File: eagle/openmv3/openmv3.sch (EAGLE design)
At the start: 64 parts, among them J3 CON_HEADER_1X03, J4 CON_HEADER_1X03, Q1 MOSFET, U12 STM32F407LQFP100, U2 USD-47571, U4 TPS768, U8 VREG_25, U9 OV2640, X2 USB-MICROB

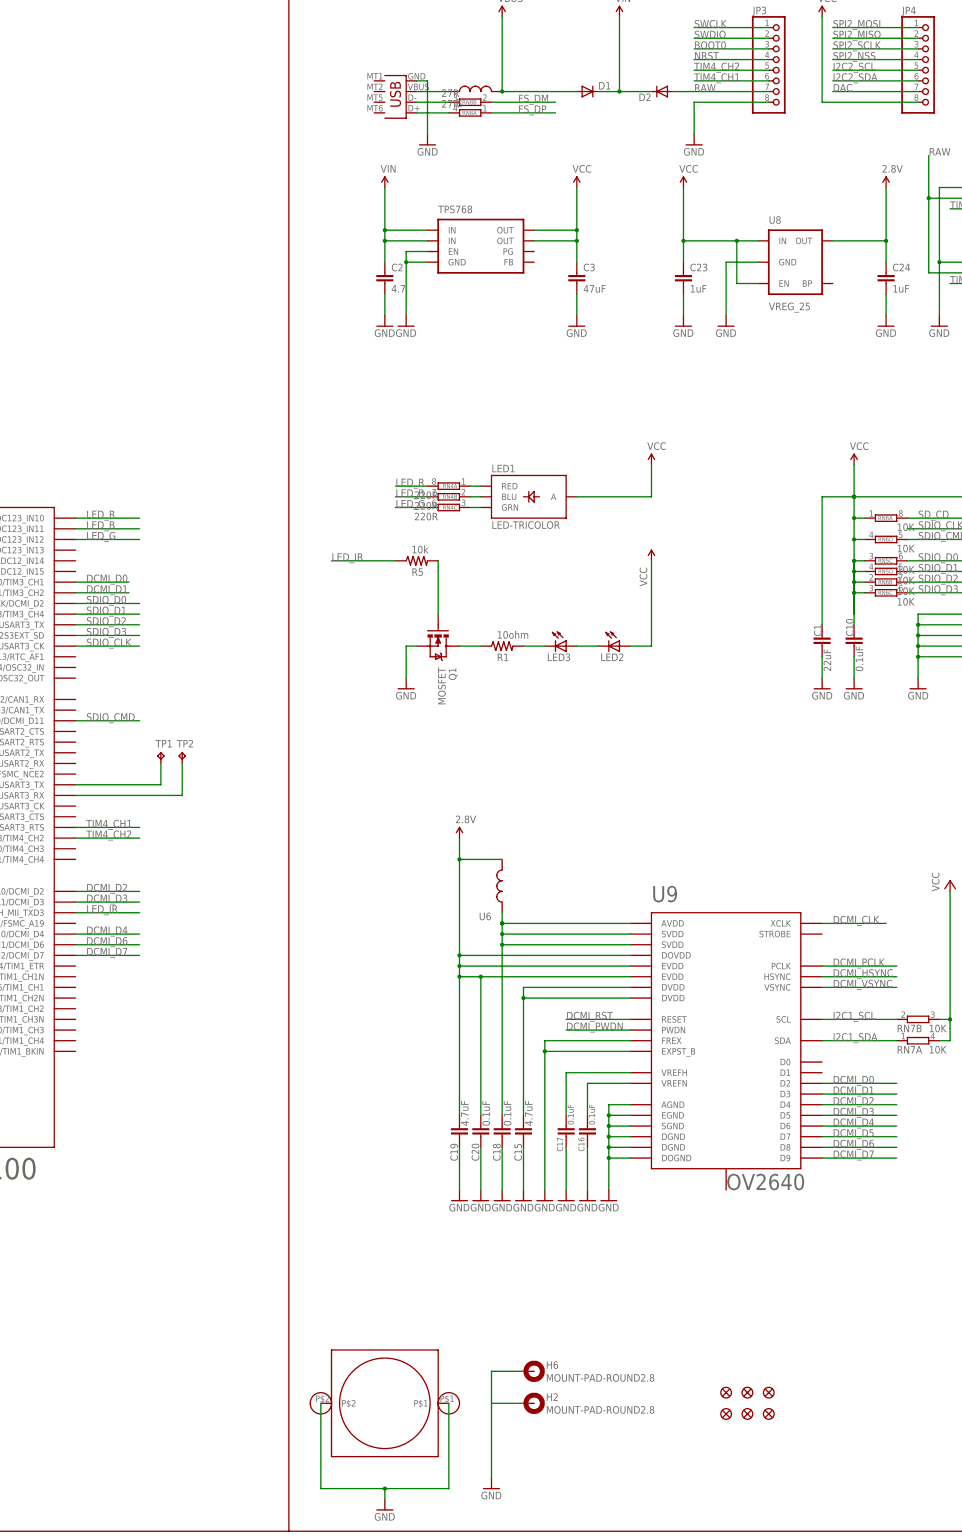
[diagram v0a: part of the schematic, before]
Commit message: Update HW
* Connect STROBE, FREX and EXPST_B
* Remove shield.
* Add pull-down to IR MOSFET
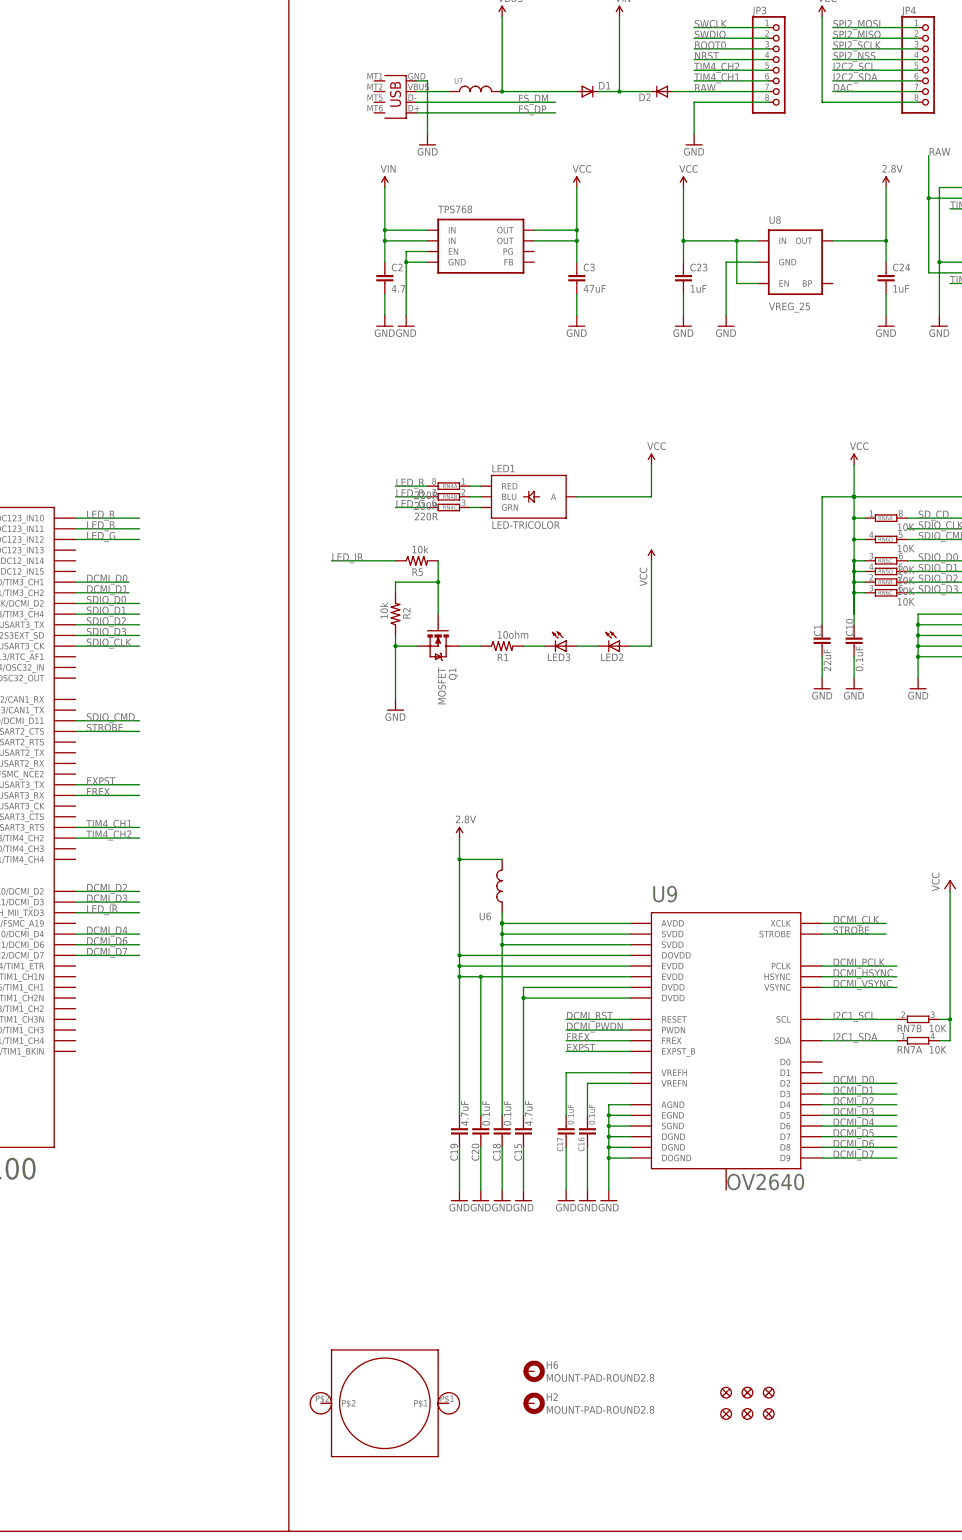
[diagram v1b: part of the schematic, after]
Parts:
- removed RN8: 27R, resistor-dil:2R-NEXBV4V
- removed TP1, TP2: TPTP12R, testpad:TPTP12R
- added R2: 10k, sfe:RESISTOR0603-RES
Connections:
- removed net N$15: RN8B.2, X2.D-
- removed net N$17: RN8A.2, X2.D+
- removed net N$19: TP1.TP, U12.PD8/FSMC_D13/USART3_TX
- removed net N$20: TP2.TP, U12.PD9/FSMC_D14/USART3_RX
- new net EXPST: U12.PD8/FSMC_D13/USART3_TX, U9.EXPST_B
- new net FREX: U12.PD9/FSMC_D14/USART3_RX, U9.FREX
- new net STROBE: U12.PD3/FSMC_CLK/USART2_CTS, U9.STROBE
- net FS_DM: now also X2.D-; no longer RN8B.1
- net FS_DP: now also X2.D+; no longer RN8A.1
- net GND: now also R2.1; no longer H2.MOUNT, H6.MOUNT, U$1.P$1, U$1.P$2, U9.EXPST_B, U9.FREX
- net N$5: now also R2.2

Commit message: Update design files
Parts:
- C2: value 4.7 -> 4.7uF
- C23, C24: value 1uF -> 4.7uF
- U8: value VREG_25 -> VREG_28
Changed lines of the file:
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@@
 <part name="GND21" library="SparkFun" deviceset="GND" device=""/>
 <part name="U$10" library="sfe" deviceset="2.8V" device=""/>
-<part name="C23" library="sfe" deviceset="CAP" device="0603-CAP" value="1uF"/>
+<part name="C23" library="sfe" deviceset="CAP" device="0603-CAP" value="4.7uF"/>
 <part name="GND27" library="SparkFun" deviceset="GND" device=""/>
-<part name="C24" library="sfe" deviceset="CAP" device="0603-CAP" value="1uF"/>
+<part name="C24" library="sfe" deviceset="CAP" device="0603-CAP" value="4.7uF"/>
 <part name="GND28" library="SparkFun" deviceset="GND" device=""/>
 <part name="U$12" library="sfe" deviceset="2.8V" device=""/>
-<part name="U8" library="sfe" deviceset="V_REG_LDO" device="SMD" value="VREG_25"/>
+<part name="U8" library="sfe" deviceset="V_REG_LDO" device="SMD" value="VREG_28"/>
 <part name="GND29" library="SparkFun" deviceset="GND" device=""/>
 <part name="P+9" library="iofault" deviceset="VIN" device=""/>
@@
 <part name="R1" library="sfe" deviceset="RESISTOR" device="0603-RES" value="10ohm"/>
 <part name="P+6" library="mux" deviceset="VCC" device=""/>
-<part name="C2" library="sfe" deviceset="CAP" device="0603-CAP" value="4.7"/>
+<part name="C2" library="sfe" deviceset="CAP" device="0603-CAP" value="4.7uF"/>
 <part name="C3" library="sfe" deviceset="CAP" device="1206" value="47uF"/>
 <part name="C11" library="sfe" deviceset="CAP" device="0805" value="22uF"/>
@@
 <instance part="C18" gate="G$1" x="304.8" y="45.72" smashed="yes">
 <attribute name="NAME" x="302.641" y="44.196" size="1.778" layer="95" rot="R270"/>
-<attribute name="VALUE" x="305.181" y="54.356" size="1.778" layer="96" rot="R270"/>
+<attribute name="VALUE" x="305.181" y="54.356" size="1.4224" layer="96" rot="R270"/>
 </instance>
 <instance part="GND17" gate="1" x="304.8" y="30.48"/>
@@
 <instance part="C19" gate="G$1" x="294.64" y="45.72" smashed="yes">
 <attribute name="NAME" x="292.481" y="44.196" size="1.778" layer="95" rot="R270"/>
-<attribute name="VALUE" x="295.021" y="54.356" size="1.778" layer="96" rot="R270"/>
+<attribute name="VALUE" x="295.021" y="54.356" size="1.4224" layer="96" rot="R270"/>
 </instance>
 <instance part="C20" gate="G$1" x="299.72" y="45.72" smashed="yes">
 <attribute name="NAME" x="297.561" y="44.196" size="1.778" layer="95" rot="R270"/>
-<attribute name="VALUE" x="300.101" y="54.356" size="1.778" layer="96" rot="R270"/>
+<attribute name="VALUE" x="300.101" y="54.356" size="1.4224" layer="96" rot="R270"/>
 </instance>
 <instance part="GND21" gate="1" x="299.72" y="30.48"/>
@@
 <instance part="C15" gate="G$1" x="309.88" y="45.72" smashed="yes">
 <attribute name="NAME" x="307.721" y="44.196" size="1.778" layer="95" rot="R270"/>
-<attribute name="VALUE" x="310.261" y="54.356" size="1.778" layer="96" rot="R270"/>
+<attribute name="VALUE" x="310.261" y="54.356" size="1.4224" layer="96" rot="R270"/>
 </instance>
 <instance part="GND12" gate="1" x="309.88" y="30.48"/>

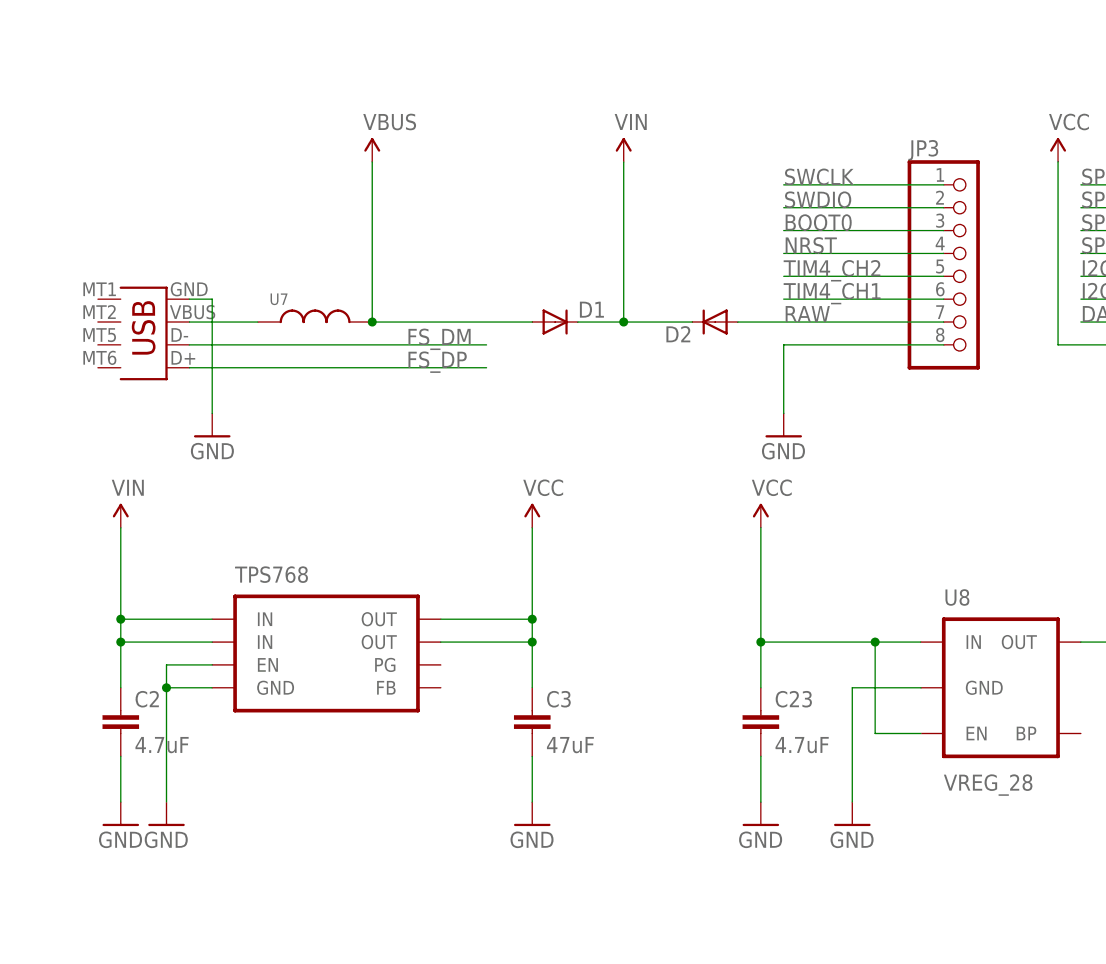
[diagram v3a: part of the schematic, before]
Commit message: Update design files
* Replace 1A TI regulator with BD 500mA.
* Replace ORing diodes with one dual common cathode.
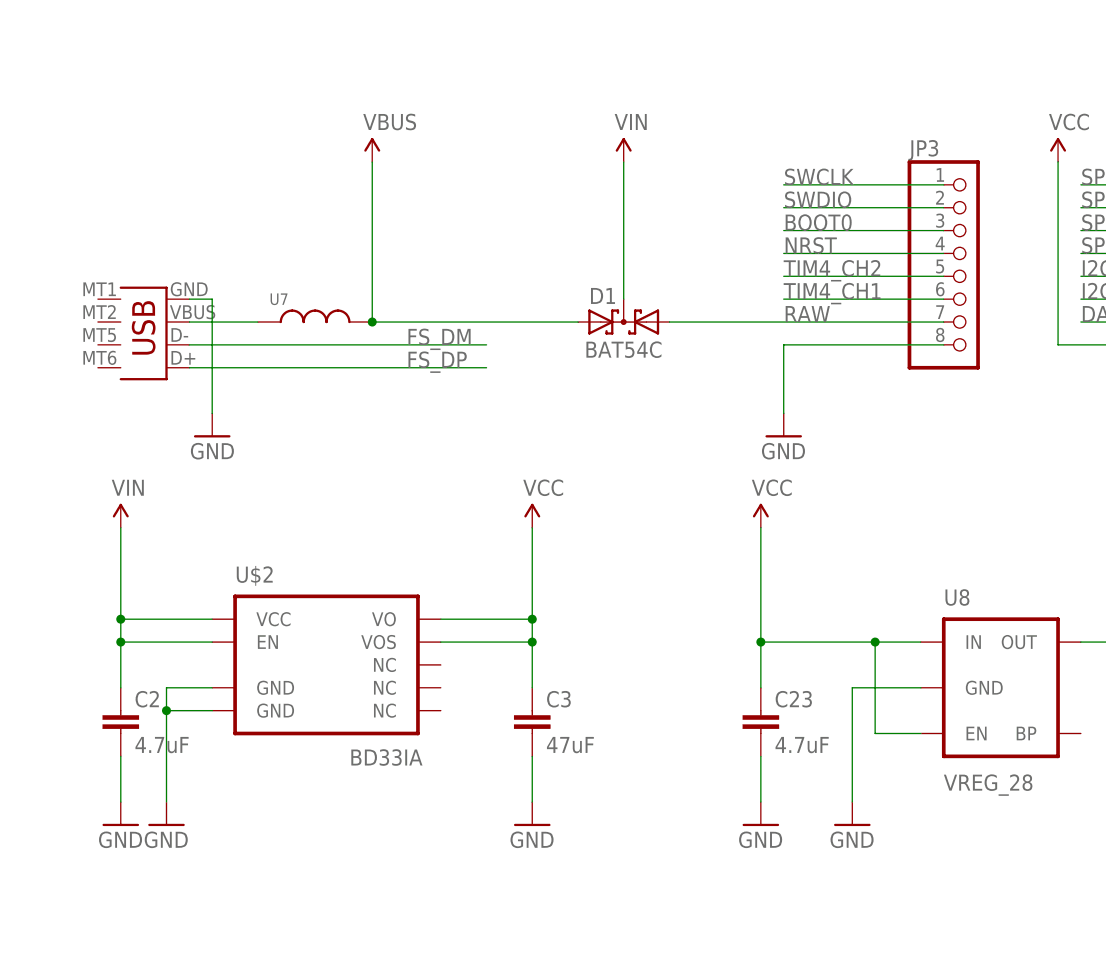
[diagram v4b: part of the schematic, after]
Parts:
- removed D2: (no value), sfe:DIODESOD
- removed U4: TPS768, mux:TPS768
- added U$2: BD33IA, mux:BD33IA
- D1: value (none) -> BAT54C; device sfe:DIODESOD -> diode:BAT54C
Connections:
- net GND: now also U$2.GND@1, U$2.GND@2; no longer U4.EN, U4.GND
- net RAW: now also D1.A1; no longer D2.A
- net VBUS: now also D1.A2; no longer D1.A
- net VCC: now also U$2.VO, U$2.VOS; no longer U4.OUT@1, U4.OUT@2
- net VIN: now also D1.CC, U$2.EN, U$2.VCC; no longer D1.C, D2.C, U4.IN@1, U4.IN@2

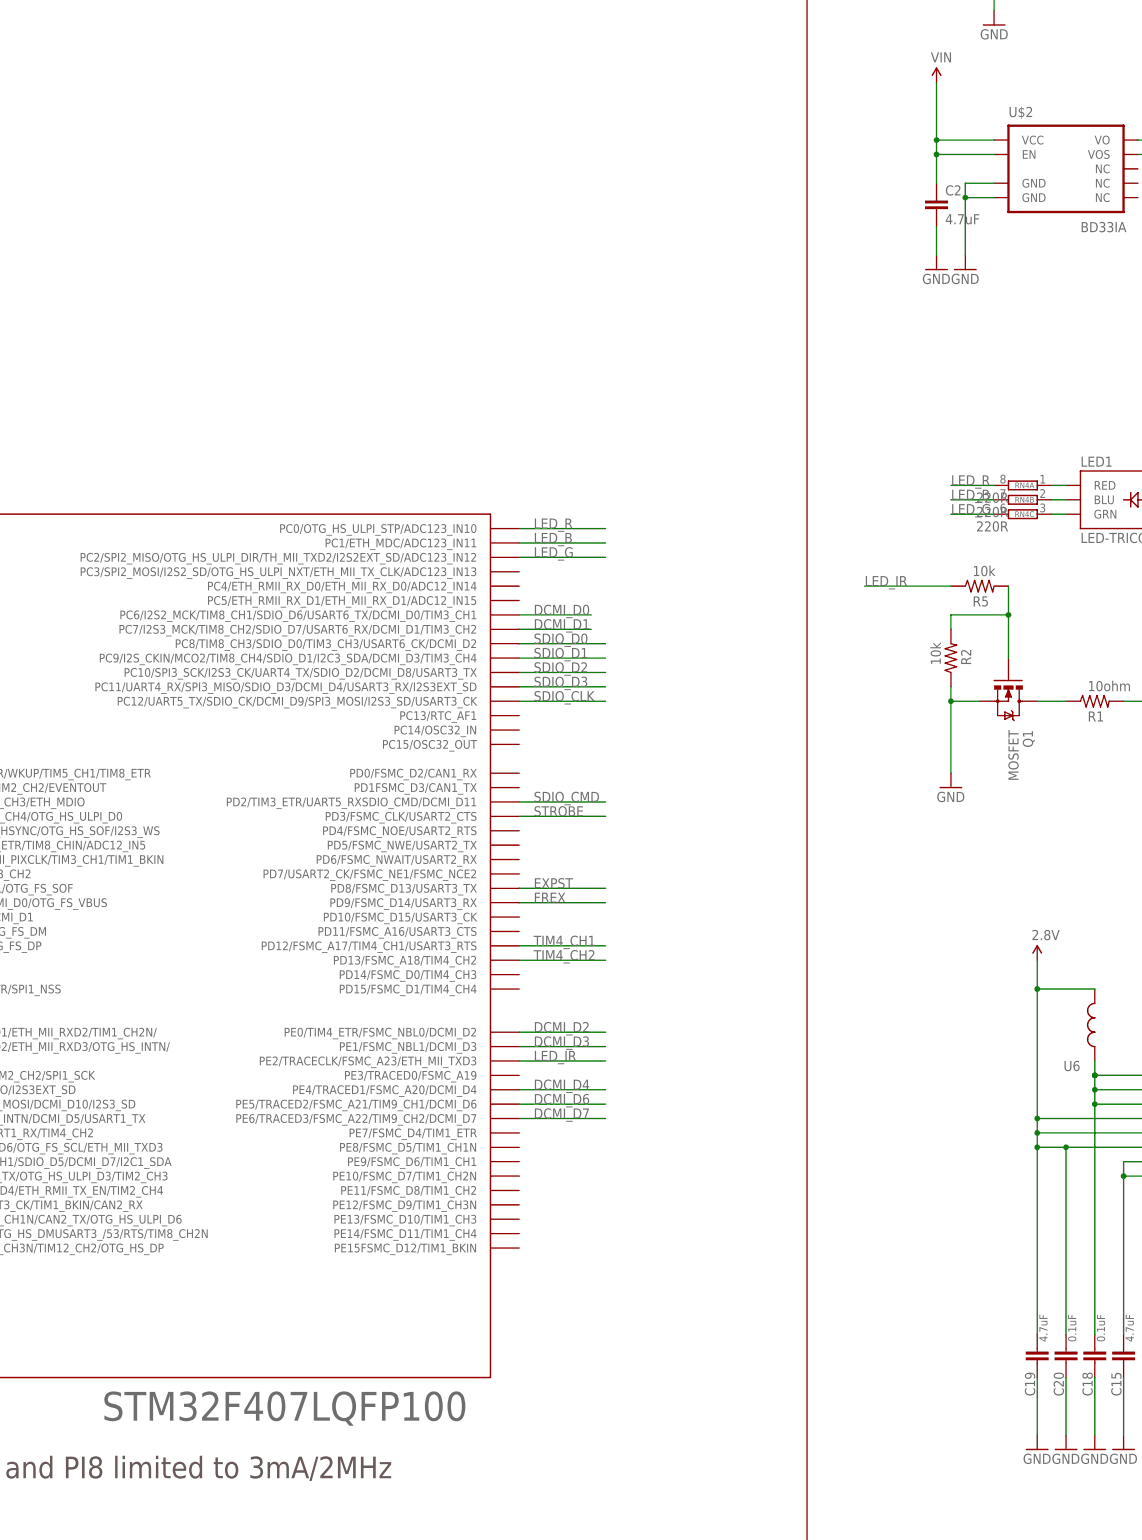
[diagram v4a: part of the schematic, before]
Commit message: Update silk screen
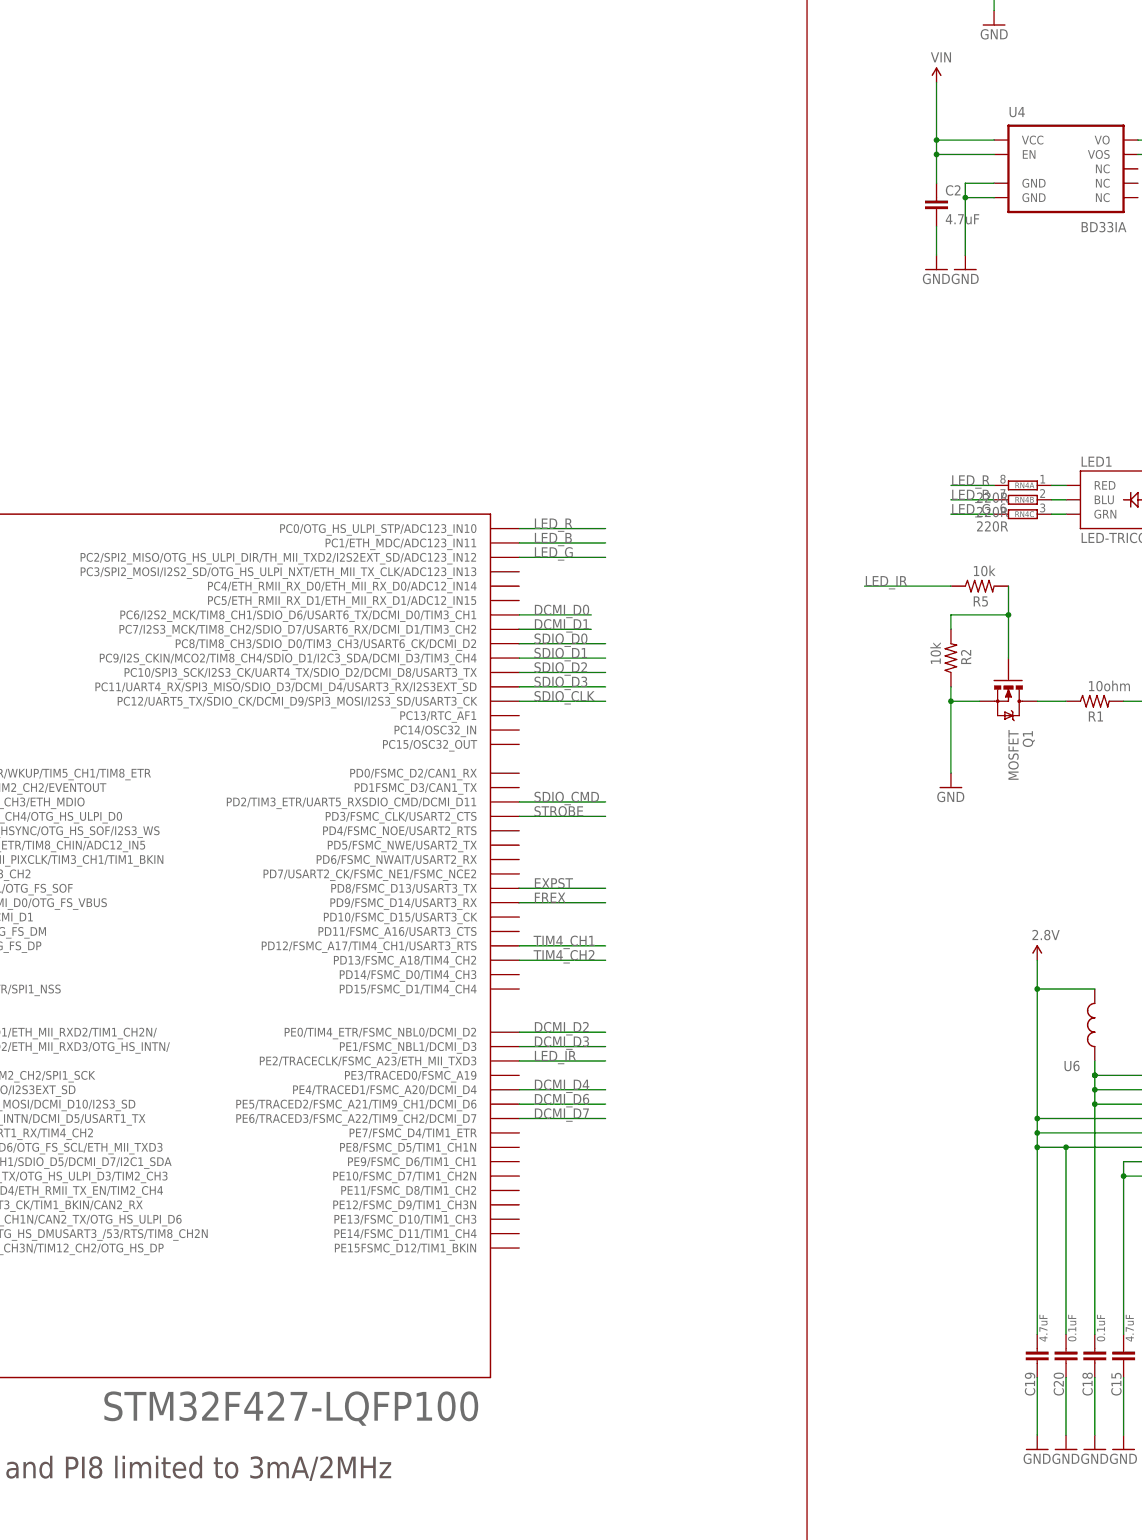
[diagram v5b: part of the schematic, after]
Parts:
- U12: value STM32F407LQFP100 -> STM32F427-LQFP100
- renumbered U$1 to U1, U$2 to U4
